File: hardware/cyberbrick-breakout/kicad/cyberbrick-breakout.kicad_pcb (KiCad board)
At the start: 2 copper layers, 85 x 70 mm, 33 parts, among them J1 LX, J10 DL_LEFT, J11 DL_RIGHT, J12 DL_DOWN, J13 DR_UP, J14 DR_LEFT, J15 DR_RIGHT, J16 DR_DOWN, J17 SHL1, J18 SHL2, J19 SHR1, J2 LY, J20 SHR2, J21 START, J22 SELECT, J23 HOTKEY, J24 COIN, J3 RX, J4 RY, J6 MCP_BTNS, J7 I2C, J8 PWR_IN, J9 DL_UP, U1A ESP32-C3 top, U1B ESP32-C3 bot

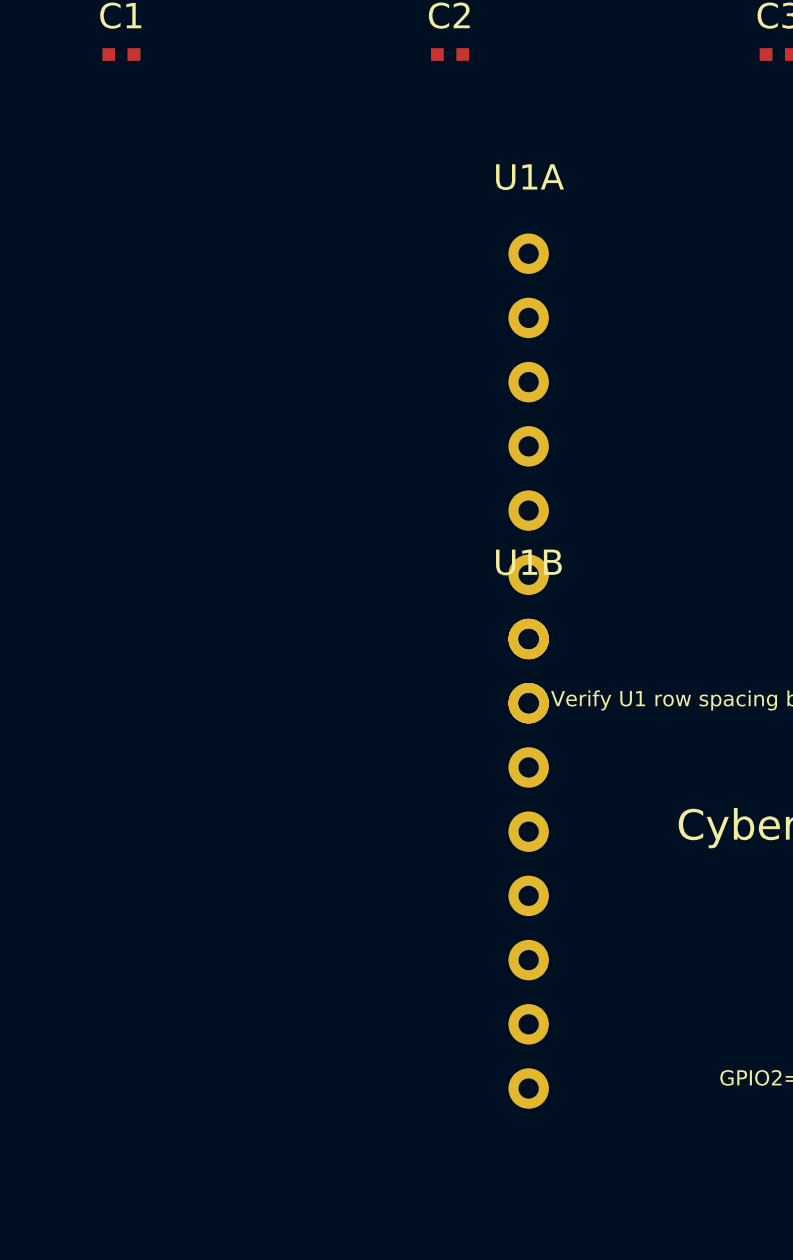
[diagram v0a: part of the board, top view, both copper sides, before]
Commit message: Fix U1 socket orientation: angle 90 so rows are horizontal, correct pin1 positions
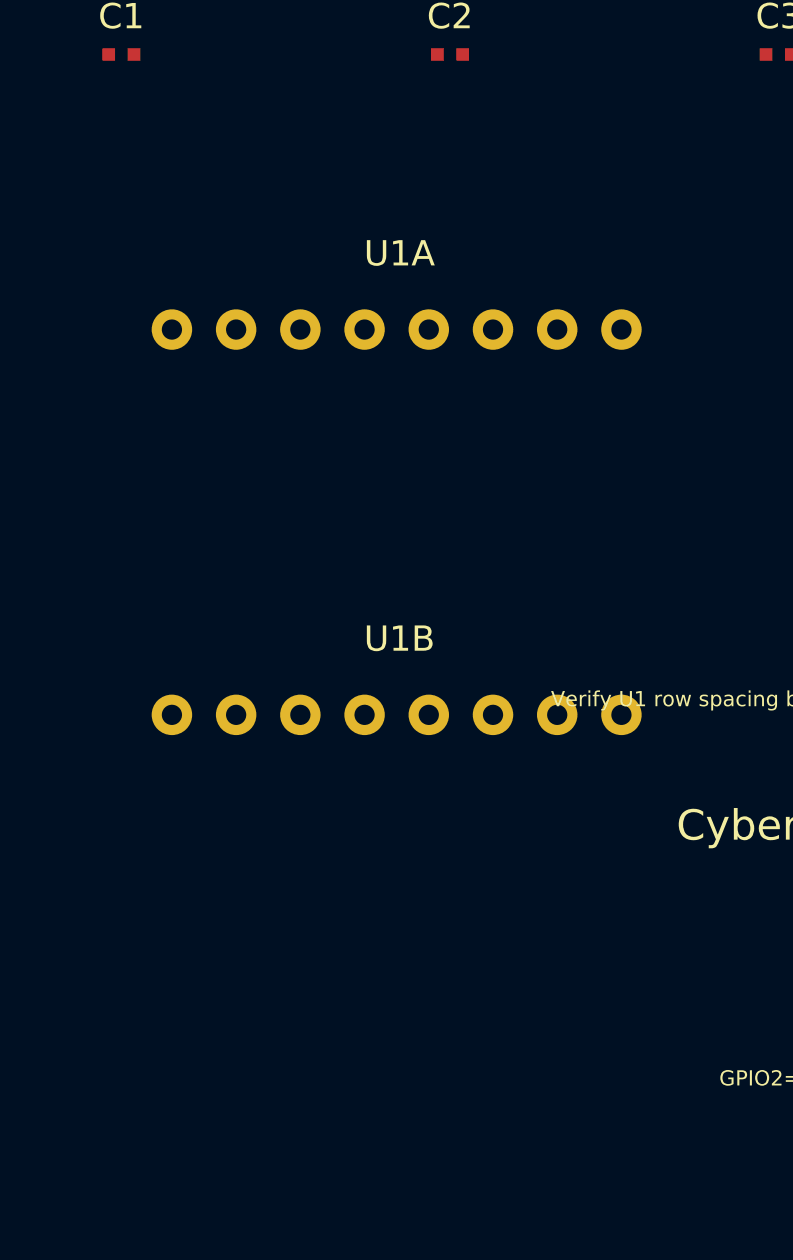
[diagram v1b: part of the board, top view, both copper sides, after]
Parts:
- moved U1A 14.4 mm to (12.0, 20.4)
- moved U1B 14.4 mm to (12.0, 35.6)
